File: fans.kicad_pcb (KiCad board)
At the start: 2 copper layers, 76.2 x 50.8 mm, 16 parts, among them M1 300, M2 300, M3 300, Q1 BC549, Q2 BC549, Q3 BC549, U2 LD1117AV33

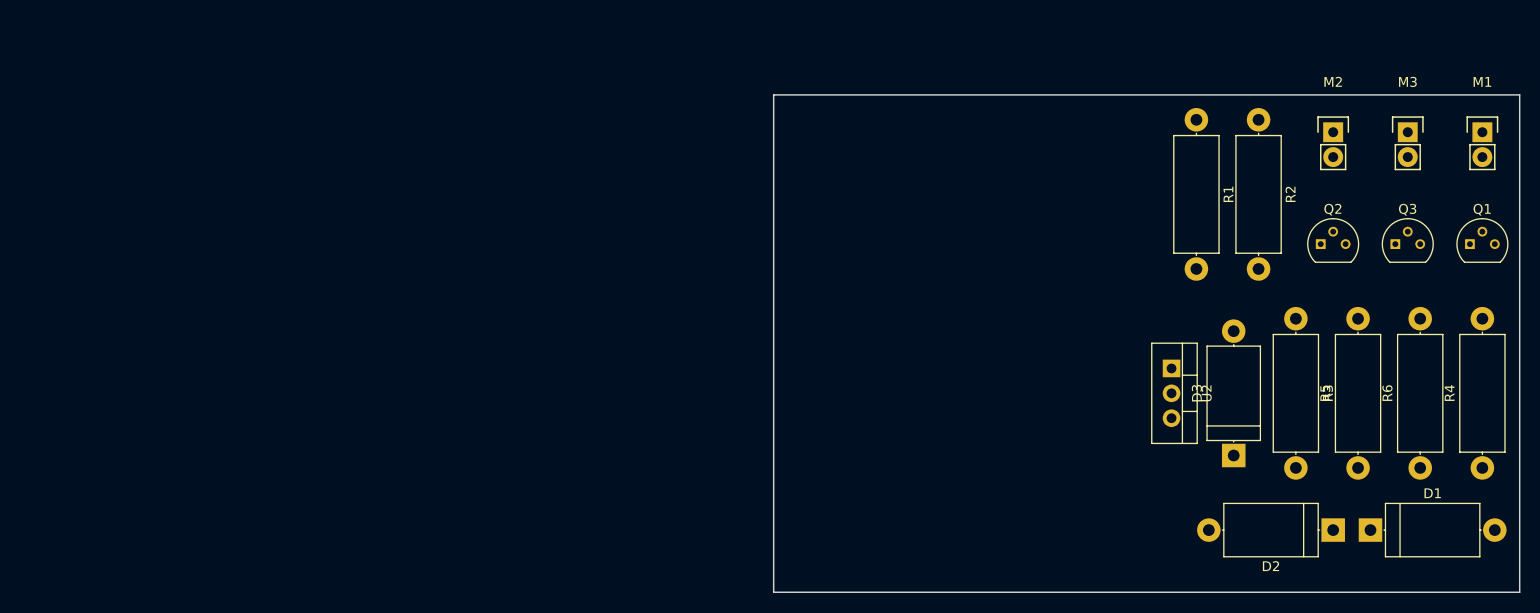
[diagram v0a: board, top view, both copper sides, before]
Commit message: Add footprint and layout
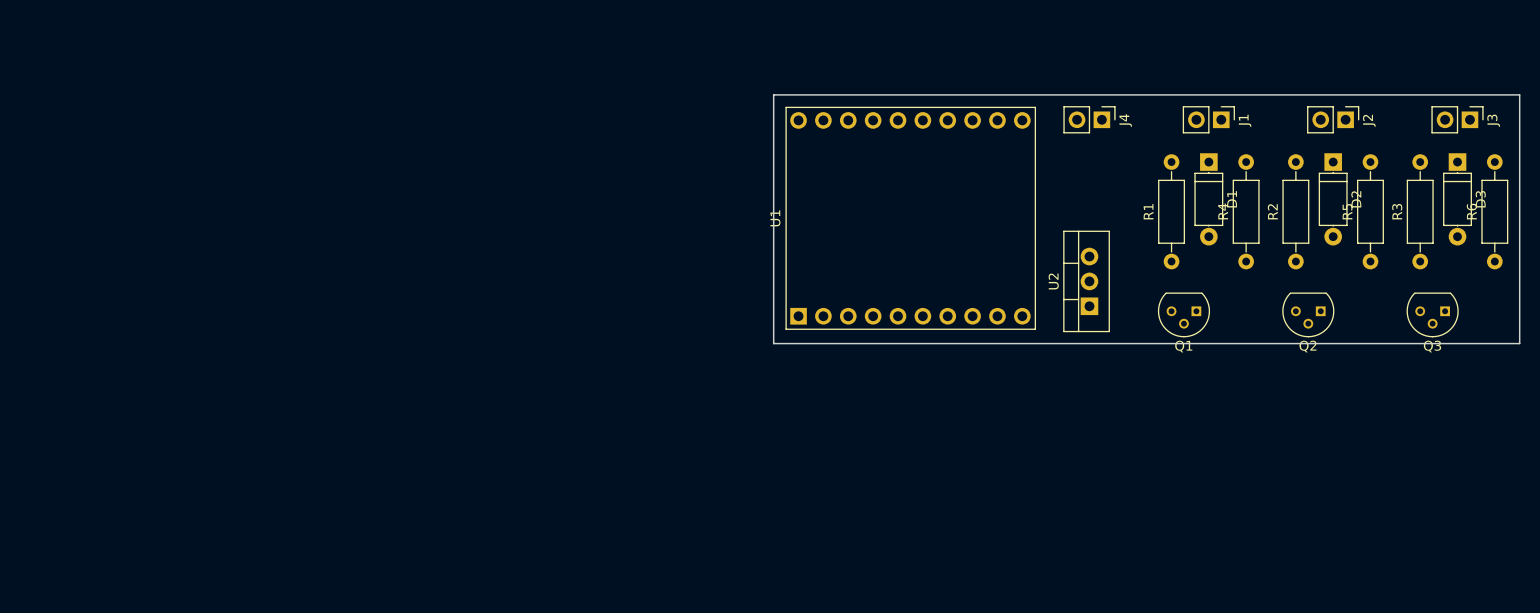
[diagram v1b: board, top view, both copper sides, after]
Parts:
- removed M1, M2, M3: 300, Pin_Headers:Pin_Header_Straight_1x02
- added J1: CONN_01X02, Pin_Headers:Pin_Header_Straight_1x02_Pitch2.54mm, F.Cu at (210.8, 71.1)
- added J2: CONN_01X02, Pin_Headers:Pin_Header_Straight_1x02_Pitch2.54mm, F.Cu at (223.5, 71.1)
- added J3: CONN_01X02, Pin_Headers:Pin_Header_Straight_1x02_Pitch2.54mm, F.Cu at (236.2, 71.1)
- added J4: CONN_01X02, Pin_Headers:Pin_Header_Straight_1x02_Pitch2.54mm, F.Cu at (198.6, 71.1)
- added U1: Adafruit_Huzzah, Adafruit_Huzzah:Adafruit_Huzzah_ESP8266_Breakout, F.Cu at (167.6, 81.2)
- D1, D2, D3: footprint Diodes_THT:D_DO-27_P12.70mm_Horizontal -> Diodes_ThroughHole:D_A-405_P7.62mm_Horizontal
- R1, R2, R3, R4, R5, R6: footprint Resistors_THT:R_Axial_DIN0414_L11.9mm_D4.5mm_P15.24mm_Horizontal -> Resistors_ThroughHole:R_Axial_DIN0207_L6.3mm_D2.5mm_P10.16mm_Horizontal
- moved D1 41.1 mm to (209.6, 75.4), turned to 270 degrees
- moved D3 37.7 mm to (234.9, 75.4), turned to 270 degrees
- moved D2 37.6 mm to (222.2, 75.4), turned to 270 degrees
- moved R4 32.0 mm to (213.4, 85.6)
- moved Q1 28.8 mm to (208.3, 90.7), turned to 180 degrees
- moved R6 22.4 mm to (238.8, 85.6)
- moved R5 21.1 mm to (226.1, 85.6)
- moved R2 15.0 mm to (218.4, 85.6), turned to 90 degrees
- moved R1 14.7 mm to (205.7, 85.6), turned to 90 degrees
- moved R3 14.0 mm to (231.1, 85.6), turned to 90 degrees
- moved U2 10.5 mm to (197.4, 90.2), turned to 90 degrees
- moved Q3 8.53 mm to (233.7, 90.7), turned to 180 degrees
- moved Q2 6.86 mm to (221.0, 90.7), turned to 180 degrees
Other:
- board size 76.2 x 50.8 mm -> 76.2 x 25.4 mm

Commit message: First finished layout.
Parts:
- moved J3 28.7 mm to (207.5, 71.1), turned to 90 degrees
- moved Q1 28.2 mm to (236.5, 90.2)
- moved D1 25.7 mm to (235.2, 75.4)
- moved D3 25.7 mm to (209.3, 75.4)
- moved R1 25.7 mm to (231.4, 85.6)
- moved R3 25.7 mm to (205.5, 85.6)
- moved R4 25.7 mm to (239.0, 85.6)
- moved R6 25.7 mm to (213.1, 85.6)
- moved Q3 23.1 mm to (210.6, 90.2)
- moved J1 23.1 mm to (233.9, 71.1), turned to 90 degrees
- moved J4 9.23 mm to (197.4, 80.3), turned to 90 degrees
- moved Q2 2.84 mm to (223.8, 90.2)
- moved J2 2.79 mm to (220.7, 71.1), turned to 90 degrees
- moved U1 0.95 mm to (167.6, 82.1)
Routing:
- net GND: track 0.00 -> 90.1 mm
- net +12V: track 0.00 -> 68.8 mm
- net Net-(R1-Pad2): track 0.00 -> 59.4 mm
- net Net-(R2-Pad2): track 0.00 -> 43.0 mm
- net Net-(R3-Pad2): track 0.00 -> 26.7 mm
- net Net-(J1-Pad2): track 0.00 -> 23.6 mm
- net Net-(J3-Pad2): track 0.00 -> 23.4 mm
- net Net-(J2-Pad2): track 0.00 -> 23.2 mm
- net +3V3: track 0.00 -> 13.8 mm
- net Net-(Q2-Pad2): track 0.00 -> 7.53 mm
- net Net-(Q3-Pad2): track 0.00 -> 7.42 mm
- net Net-(Q1-Pad2): track 0.00 -> 7.42 mm
- net Net-(D2-Pad2): track 0.00 -> 4.86 mm
- net Net-(D1-Pad2): track 0.00 -> 4.86 mm
- net Net-(D3-Pad2): track 0.00 -> 4.86 mm
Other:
- board size 76.2 x 25.4 mm -> 76.2 x 27.9 mm
- net class Default: clearance 0.2 -> 0.4; trace_width 0.25 -> 0.4; via_dia 0.6 -> 2.5; via_drill 0.4 -> 1
- rule trace_clearance: 0.2 -> 0.4
- rule trace_min: 0.2 -> 0.4
- rule via_min_size: 0.4 -> 2.5

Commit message: Wider traces.
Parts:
- Q1, Q2, Q3: footprint TO_SOT_Packages_THT:TO-92_Molded_Narrow -> TO_SOT_Packages_THT:TO-92_Molded_Wide_Oval
- moved Q1 79.2 mm to (157.5, 85.1), turned to 0 degrees
- moved Q2 79.2 mm to (144.8, 85.1), turned to 0 degrees
- moved Q3 78.9 mm to (131.8, 85.1), turned to 0 degrees
- moved D1 76.4 mm to (159.0, 70.4)
- moved R1 76.4 mm to (155.2, 80.5)
- moved R4 76.4 mm to (162.8, 80.5)
- moved J4 76.4 mm to (121.2, 75.2)
- moved U2 76.4 mm to (121.2, 85.1)
- moved D2 76.4 mm to (146.1, 70.4)
- moved D3 76.4 mm to (133.1, 70.4)
- moved J1 76.4 mm to (157.7, 66.0)
- moved J2 76.4 mm to (144.5, 66.0)
- moved J3 76.4 mm to (131.3, 66.0)
- moved R2 76.4 mm to (142.2, 80.5)
- moved R3 76.4 mm to (129.3, 80.5)
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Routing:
- net Net-(J2-Pad2): track 23.2 -> 31.1 mm
- net Net-(J1-Pad2): track 23.6 -> 29.7 mm
- net Net-(J3-Pad2): track 23.4 -> 28.7 mm
- net Net-(Q1-Pad2): track 7.42 -> 5.92 mm
- net Net-(Q2-Pad2): track 7.53 -> 6.07 mm
- net Net-(Q3-Pad2): track 7.42 -> 6.07 mm
- net Net-(R3-Pad2): track 26.7 -> 25.9 mm
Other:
- net class Default: clearance 0.4 -> 0.6; trace_width 0.4 -> 0.6
- rule trace_clearance: 0.4 -> 0.6
